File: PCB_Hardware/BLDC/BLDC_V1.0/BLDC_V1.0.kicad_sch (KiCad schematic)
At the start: 0 parts

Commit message: Removed external temp sensing bc I forgot the calibration enable pin for the encoder
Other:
- sheet MCU ports: added CAL_EN; removed EXT_TEMP
- sheet Temp Sense ports: added none; removed EXT_TEMP
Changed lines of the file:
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@@
-	(wire
-		(pts
-			(xy 203.2 152.4) (xy 215.9 152.4)
-		)
-		(stroke
-			(width 0)
-			(type default)
-		)
-	)
 	(wire
 		(pts
@@
 		(pts
 			(xy 203.2 212.09) (xy 215.9 212.09)
+		)
+		(stroke
+			(width 0)
+			(type default)
+		)
+	)
+	(wire
+		(pts
+			(xy 203.2 123.19) (xy 215.9 123.19)
 		)
 		(stroke
@@
 			)
 		)
-		(pin "EXT_TEMP" input
-			(at 215.9 152.4 180)
-			(effects
-				(font
-					(size 1.27 1.27)
-				)
-				(justify left)
-			)
-		)
 		(instances
 			(project "BLDC_V1.0"
@@
 			)
 		)
-		(pin "EXT_TEMP" input
-			(at 203.2 152.4 0)
-			(effects
-				(font
-					(size 1.27 1.27)
-				)
-				(justify right)
-			)
-		)
 		(pin "VBUS" input
 			(at 127 66.04 180)
@@
 			)
 		)
+		(pin "CAL_EN" input
+			(at 203.2 123.19 0)
+			(effects
+				(font
+					(size 1.27 1.27)
+				)
+				(justify right)
+			)
+		)

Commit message: redid external temp sensing and instead removed V Bus sense from the USBC input
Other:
- sheet MCU ports: added EXT_TEMP; removed CAL_EN, VBUS
- sheet Temp Sense ports: added EXT_TEMP; removed none
- sheet USBC ports: added none; removed VBUS
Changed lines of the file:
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@@
+	(wire
+		(pts
+			(xy 203.2 152.4) (xy 215.9 152.4)
+		)
+		(stroke
+			(width 0)
+			(type default)
+		)
+	)
 	(wire
 		(pts
@@
 	(wire
 		(pts
-			(xy 203.2 123.19) (xy 215.9 123.19)
-		)
-		(stroke
-			(width 0)
-			(type default)
-		)
-	)
-	(wire
-		(pts
 			(xy 63.5 104.14) (xy 127 104.14)
 		)
@@
 		(pts
 			(xy 203.2 64.77) (xy 215.9 64.77)
-		)
-		(stroke
-			(width 0)
-			(type default)
-		)
-	)
-	(wire
-		(pts
-			(xy 63.5 66.04) (xy 127 66.04)
 		)
 		(stroke
@@
 			)
 		)
+		(pin "EXT_TEMP" input
+			(at 215.9 152.4 180)
+			(effects
+				(font
+					(size 1.27 1.27)
+				)
+				(justify left)
+			)
+		)
 		(instances
 			(project "BLDC_V1.0"
@@
 			)
 		)
-		(pin "VBUS" input
-			(at 63.5 66.04 0)
-			(effects
-				(font
-					(size 1.27 1.27)
-				)
-				(justify right)
-			)
-		)
 		(instances
 			(project "BLDC_V1.0"
@@
 			)
 		)
-		(pin "VBUS" input
-			(at 127 66.04 180)
-			(effects
-				(font
-					(size 1.27 1.27)
-				)
-				(justify left)
+		(pin "EXT_TEMP" input
+			(at 203.2 152.4 0)
+			(effects
+				(font
+					(size 1.27 1.27)
+				)
+				(justify right)
 			)
 		)
@@
 			)
 		)
-		(pin "CAL_EN" input
-			(at 203.2 123.19 0)
-			(effects
-				(font
-					(size 1.27 1.27)
-				)
-				(justify right)
-			)
-		)

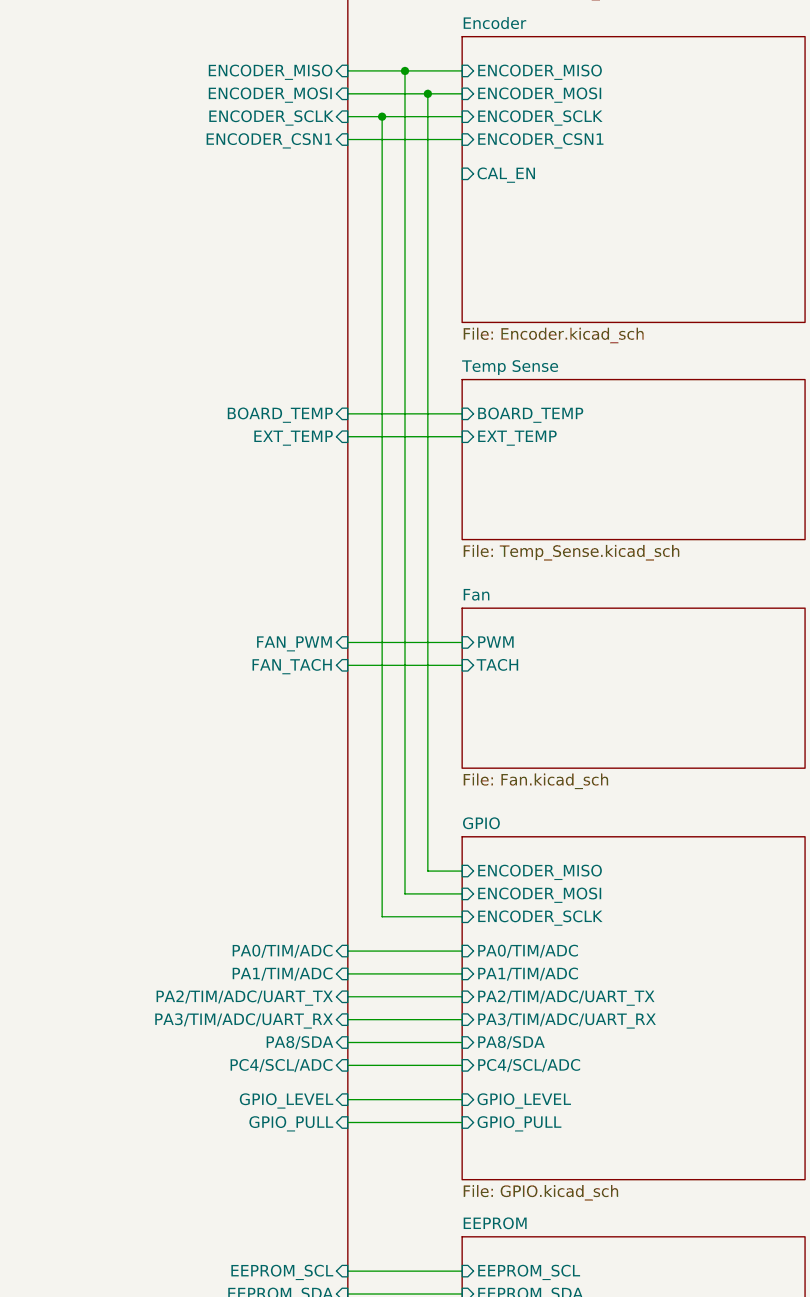
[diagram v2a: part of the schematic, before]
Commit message: foget to add the GPIO to change the voltage for AUX2 SPI port, removed the ability to pull AUX pins down to free a pin
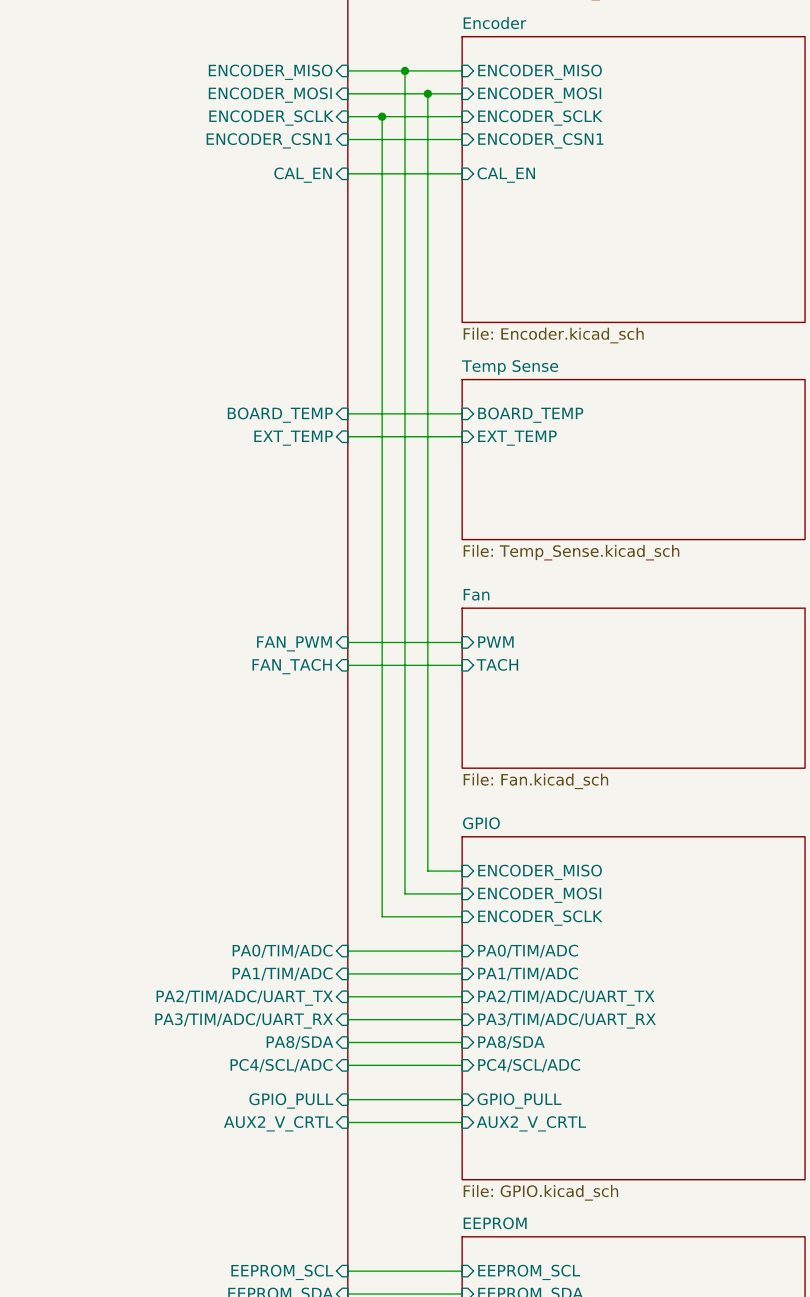
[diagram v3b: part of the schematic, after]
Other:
- sheet GPIO ports: added AUX2_V_CRTL; removed GPIO_LEVEL
- sheet MCU ports: added AUX2_V_CRTL, CAL_EN; removed GPIO_LEVEL
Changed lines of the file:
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@@
+	(wire
+		(pts
+			(xy 203.2 228.6) (xy 215.9 228.6)
+		)
+		(stroke
+			(width 0)
+			(type default)
+		)
+	)
 	(wire
 		(pts
@@
 	(wire
 		(pts
+			(xy 63.5 31.75) (xy 127 31.75)
+		)
+		(stroke
+			(width 0)
+			(type default)
+		)
+	)
+	(wire
+		(pts
+			(xy 203.2 49.53) (xy 215.9 49.53)
+		)
+		(stroke
+			(width 0)
+			(type default)
+		)
+	)
+	(wire
+		(pts
+			(xy 203.2 52.07) (xy 215.9 52.07)
+		)
+		(stroke
+			(width 0)
+			(type default)
+		)
+	)
+	(wire
+		(pts
+			(xy 203.2 247.65) (xy 215.9 247.65)
+		)
+		(stroke
+			(width 0)
+			(type default)
+		)
+	)
+	(wire
+		(pts
+			(xy 203.2 69.85) (xy 215.9 69.85)
+		)
+		(stroke
+			(width 0)
+			(type default)
+		)
+	)
+	(wire
+		(pts
+			(xy 203.2 35.56) (xy 215.9 35.56)
+		)
+		(stroke
+			(width 0)
+			(type default)
+		)
+	)
+	(wire
+		(pts
+			(xy 203.2 116.84) (xy 207.01 116.84)
+		)
+		(stroke
+			(width 0)
+			(type default)
+		)
+	)
+	(wire
+		(pts
+			(xy 203.2 111.76) (xy 209.55 111.76)
+		)
+		(stroke
+			(width 0)
+			(type default)
+		)
+	)
+	(wire
+		(pts
+			(xy 63.5 36.83) (xy 127 36.83)
+		)
+		(stroke
+			(width 0)
+			(type default)
+		)
+	)
+	(wire
+		(pts
 			(xy 203.2 226.06) (xy 215.9 226.06)
 		)
@@
 	(wire
 		(pts
-			(xy 203.2 228.6) (xy 215.9 228.6)
-		)
-		(stroke
-			(width 0)
-			(type default)
-		)
-	)
-	(wire
-		(pts
-			(xy 63.5 31.75) (xy 127 31.75)
-		)
-		(stroke
-			(width 0)
-			(type default)
-		)
-	)
-	(wire
-		(pts
-			(xy 203.2 49.53) (xy 215.9 49.53)
-		)
-		(stroke
-			(width 0)
-			(type default)
-		)
-	)
-	(wire
-		(pts
-			(xy 203.2 52.07) (xy 215.9 52.07)
-		)
-		(stroke
-			(width 0)
-			(type default)
-		)
-	)
-	(wire
-		(pts
-			(xy 203.2 247.65) (xy 215.9 247.65)
-		)
-		(stroke
-			(width 0)
-			(type default)
-		)
-	)
-	(wire
-		(pts
-			(xy 203.2 69.85) (xy 215.9 69.85)
-		)
-		(stroke
-			(width 0)
-			(type default)
-		)
-	)
-	(wire
-		(pts
-			(xy 203.2 35.56) (xy 215.9 35.56)
-		)
-		(stroke
-			(width 0)
-			(type default)
-		)
-	)
-	(wire
-		(pts
-			(xy 203.2 116.84) (xy 207.01 116.84)
-		)
-		(stroke
-			(width 0)
-			(type default)
-		)
-	)
-	(wire
-		(pts
-			(xy 203.2 111.76) (xy 209.55 111.76)
-		)
-		(stroke
-			(width 0)
-			(type default)
-		)
-	)
-	(wire
-		(pts
-			(xy 63.5 36.83) (xy 127 36.83)
-		)
-		(stroke
-			(width 0)
-			(type default)
-		)
-	)
-	(wire
-		(pts
 			(xy 203.2 217.17) (xy 215.9 217.17)
 		)
@@
 		(pts
 			(xy 203.2 64.77) (xy 215.9 64.77)
+		)
+		(stroke
+			(width 0)
+			(type default)
+		)
+	)
+	(wire
+		(pts
+			(xy 203.2 123.19) (xy 215.9 123.19)
 		)
 		(stroke
@@
 			)
 		)
-		(pin "GPIO_LEVEL" input
-			(at 215.9 226.06 180)
-			(effects
-				(font
-					(size 1.27 1.27)
-				)
-				(justify left)
-			)
-		)
-		(pin "GPIO_PULL" input
-			(at 215.9 228.6 180)
-			(effects
-				(font
-					(size 1.27 1.27)
-				)
-				(justify left)
-			)
-		)
 		(pin "PA0{slash}TIM{slash}ADC" input
 			(at 215.9 209.55 180)
@@
 		(pin "PC4{slash}SCL{slash}ADC" input
 			(at 215.9 222.25 180)
+			(effects
+				(font
+					(size 1.27 1.27)
+				)
+				(justify left)
+			)
+		)
+		(pin "AUX2_V_CRTL" input
+			(at 215.9 228.6 180)
+			(effects
+				(font
+					(size 1.27 1.27)
+				)
+				(justify left)
+			)
+		)
+		(pin "GPIO_PULL" input
+			(at 215.9 226.06 180)
 			(effects
 				(font
@@
 			)
 		)
-		(pin "GPIO_LEVEL" input
-			(at 203.2 226.06 0)
-			(effects
-				(font
-					(size 1.27 1.27)
-				)
-				(justify right)
-			)
-		)
-		(pin "GPIO_PULL" input
-			(at 203.2 228.6 0)
-			(effects
-				(font
-					(size 1.27 1.27)
-				)
-				(justify right)
-			)
-		)
 		(pin "PA0{slash}TIM{slash}ADC" input
 			(at 203.2 209.55 0)
@@
 			)
 		)
+		(pin "CAL_EN" input
+			(at 203.2 123.19 0)
+			(effects
+				(font
+					(size 1.27 1.27)
+				)
+				(justify right)
+			)
+		)
+		(pin "AUX2_V_CRTL" input
+			(at 203.2 228.6 0)
+			(effects
+				(font
+					(size 1.27 1.27)
+				)
+				(justify right)
+			)
+		)
+		(pin "GPIO_PULL" input
+			(at 203.2 226.06 0)
+			(effects
+				(font
+					(size 1.27 1.27)
+				)
+				(justify right)
+			)
+		)
